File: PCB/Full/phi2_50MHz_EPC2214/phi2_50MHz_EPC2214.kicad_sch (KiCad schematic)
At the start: 37 parts, among them J4 RF_IN, J5 Conn_01x01_Pin, J6 Conn_01x01_Pin, Q1 EPC2051, Q2 EPC2051, Q3 GS61004B-MR, U1 LMG1020YFF, U1 TLV3501, U11 LMG1020YFF, U3 NC7WZ04, U5 NC7WZ04, U6 NC7WZ04, U7 NC7WZ04

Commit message: some progress on 50 MHz design
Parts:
- removed J4: RF_IN, Connector_Coaxial:SMA_Amphenol_132134-10_Vertical, symbol Connector:Conn_Coaxial
- removed Q1, Q2: EPC2051, EPCGaN:BGA-6_3x2_6.0x6.0mm, symbol Device:Q_NMOS_GSD
- removed U1: TLV3501, Package_TO_SOT_SMD:SOT-23-6, symbol MyKICAD:TLV3501
- removed U1: LMG1020YFF, GateDriver:BGA6N40P3X2_125X85X62N, symbol Driver_FET:LMG1020YFF
- added C11: C_Small, Capacitor_SMD:C_0402_1005Metric, symbol Device:C_Small
- added C12, C13, C15, C19, C20, C21, C22, C5: C, symbol Device:C_Small
- added C18: C_Small, Capacitor_SMD:CP_Elec_10x10, symbol Device:C_Small
- added C23, C24: 10U, Capacitor_SMD:C_0805_2012Metric, symbol Device:C_Small
- added C25: 100n, Capacitor_SMD:C_0603_1608Metric, symbol Device:C_Small
- added C26, C27, C28: 22U, Capacitor_SMD:C_1206_3216Metric, symbol Device:C_Small
- added C29: 100N, Capacitor_SMD:C_0603_1608Metric, symbol Device:C_Small
- added FL1: Choke, Coilcraft:IND_LPD4012-103MRB, symbol Filter:Choke_Schaffner_RN102-0.3-02-12M
- added J2: RF_IN, Connector_Coaxial:SMA_Amphenol_132134-10_Vertical, symbol Connector:Conn_Coaxial
- added L1, L2, L3, L4: L, symbol Device:L
- added L5: 2.2U, Inductor_SMD:L_Taiyo-Yuden_MD-5050, symbol Device:L_Small
- added Q2: GS61004B-MR, EPCGaN:TRANS_GS61004B-MR, symbol GS61004B-MR:GS61004B-MR
- added R13, R14: 1, Resistor_SMD:R_0402_1005Metric, symbol Device:R_Small_US
- added R7: 30K, Resistor_SMD:R_0603_1608Metric, symbol Device:R_Small_US
- added U1: TPS565242, Package_TO_SOT_SMD:SOT-563, symbol MyKICAD:TPS565242
- C1, C10, C16, C2, C3, C4: footprint Capacitor_SMD:C_0603_1608Metric_Pad1.08x0.95mm_HandSolder -> Capacitor_SMD:C_0603_1608Metric
- C14: footprint Capacitor_SMD:C_0603_1608Metric_Pad1.08x0.95mm_HandSolder -> Capacitor_SMD:C_0402_1005Metric
- C17, C8, C9: footprint Capacitor_SMD:C_0402_1005Metric_Pad0.74x0.62mm_HandSolder -> Capacitor_SMD:C_0402_1005Metric
- C6, C7: value C_Small -> C; footprint Capacitor_SMD:C_0402_1005Metric_Pad0.74x0.62mm_HandSolder -> (none)
- Q3: footprint GS61004B-MR:TRANS_GS61004B-MR -> EPCGaN:TRANS_GS61004B-MR
- R1: value 50 -> 100K; footprint Resistor_SMD:R_0603_1608Metric -> Resistor_SMD:R_0402_1005Metric
- R2: value OPEN -> 15K; footprint Resistor_SMD:R_0603_1608Metric -> Resistor_SMD:R_0402_1005Metric
- R3: value SHORT -> 220K
- U3, U5, U6, U7: footprint pcbparts:SOIC-6 -> pcbparts:nc7wz04_sc-88_SOIC-6
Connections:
- net RF_IN_4 is gone; now on net RF_IN: R1.2, U1.3 (+IN)
- net +5V: now also C8.2, C9.2, C11.2; no longer C1.1, C2.1, C3.1, C4.1, C6.1, C7.1, C8.1, C9.1, J5.1 (Pin_1), R2.1
- net GND: now also C8.1, C9.1, R2.2, C11.1, C12.2, C13.2, C15.2, C18.2, C19.2, C20.2, C21.2, C22.2, C23.2, C24.2, C25.2, C26.2, C27.2, C28.2, C29.2, C5.2, FL1.4, J2.2 (Ext), Q2.3, R7.2, U1.3 (GND), U1.4 (AGND); no longer C8.2, C9.2, R1.1, R3.2, U3.3 (A2), U5.4 (Y2), U6.4 (Y2), U7.4 (Y2)
- net at U5.6 (Y1), U6.6 (Y1), U7.6 (Y1): now also U5.4 (Y2), U6.4 (Y2), U7.4 (Y2), R14.1
- net 5V: now reaches R3.1
- net 5V: now also C26.1, C27.1, C28.1, C29.1, L5.2; no longer R2.2
- net at U11.A2 (OUTH), U11.B2 (OUTL): now also R13.1; no longer Q3.2
- net BUFF_OUT+: no longer names the net of U3.6 (Y1), U5.1 (A1), U6.1 (A1), U7.1 (A1)
- net BUFF_OUT+: now also U5.3 (A2), U6.3 (A2), U7.3 (A2)
- removed net BUFF_OUT-: U3.4 (Y2), U5.3 (A2), U6.3 (A2), U7.3 (A2)
- net RF_IN_1: no longer names the net of R1.2
- net RF_IN_1: now also R2.1, U1.5 (EN); no longer J4.1 (In)
- net RF_IN_2 renamed RF_IN
- net RF_IN: now also J4.1 (In)
- new net: Q3.2, R13.2
- new net: C13.1, C5.1, C6.1, C7.1, L2.2
- new net: C15.1, C19.1, C20.1, L1.2, L2.1, L3.1, Q2.1
- new net: L5.1, U1.2 (SW)
- new net: C12.1, C21.1, C22.1, L3.2, L4.1
- new net: R3.2, R7.1, U1.6 (FB)
- new net: J2.1 (In), L4.2
- new net +12V: C1.1, C18.1, C2.1, C3.1, C4.1, FL1.1, J5.1 (Pin_1), L1.1
- new net 12V: C23.1, C24.1, C25.1, FL1.2, R1.1, U1.1 (VIN)
- new net G: Q2.2, R14.2
- new net GND_IN: FL1.3
- no-connect marks 0 -> 2
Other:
- moved on the sheet: C1, C10, C14, C16, C17, C2, C3, C4, R1, R2, R3, U1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

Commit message: small schem progress
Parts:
- C11, C8, C9: value C_Small -> C
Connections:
- net 5V is gone; now on net +5V: C26.1, C27.1, C28.1, C29.1, L5.2, R3.1
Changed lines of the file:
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@@
 	)
 	(junction
+		(at 162.56 74.93)
+		(diameter 0)
+		(color 0 0 0 0)
+	)
+	(junction
 		(at 110.49 138.43)
 		(diameter 0)
@@
 	(wire
 		(pts
+			(xy 162.56 73.66) (xy 162.56 74.93)
+		)
+		(stroke
+			(width 0)
+			(type default)
+		)
+	)
+	(wire
+		(pts
 			(xy 217.17 148.59) (xy 217.17 149.86)
 		)
@@
 		)
 	)
-	(label "5V"
-		(at 162.56 74.93 0)
-		(fields_autoplaced yes)
-		(effects
-			(font
-				(size 1.27 1.27)
-			)
-			(justify left bottom)
-		)
-	)
 	(label "RF_IN"
 		(at 203.2 139.7 180)
@@
 			)
 		)
-		(property "Value" "C_Small"
-			(at 130.81 120.65 0)
+		(property "Value" "C"
+			(at 137.668 121.158 0)
 			(effects
 				(font
@@
 	)
 	(symbol
+		(lib_id "power:+5V")
+		(at 162.56 73.66 0)
+		(unit 1)
+		(exclude_from_sim no)
+		(in_bom yes)
+		(on_board yes)
+		(dnp no)
+		(property "Reference" "#PWR06"
+			(at 162.56 77.47 0)
+			(effects
+				(font
+					(size 1.27 1.27)
+				)
+				(hide yes)
+			)
+		)
+		(property "Value" "+5V"
+			(at 160.02 69.85 0)
+			(effects
+				(font
+					(size 1.27 1.27)
+				)
+				(justify left)
+			)
+		)
+		(property "Footprint" ""
+			(at 162.56 73.66 0)
+			(effects
+				(font
+					(size 1.27 1.27)
+				)
+				(hide yes)
+			)
+		)
+		(property "Datasheet" ""
+			(at 162.56 73.66 0)
+			(effects
+				(font
+					(size 1.27 1.27)
+				)
+				(hide yes)
+			)
+		)
+		(property "Description" ""
+			(at 162.56 73.66 0)
+			(effects
+				(font
+					(size 1.27 1.27)
+				)
+				(hide yes)
+			)
+		)
+		(pin "1"
+		)
+		(instances
+			(project "phi2_50MHz_EPC2214"
+				(path "/f0e94b14-ee89-4887-b170-fe37e788a393"
+					(reference "#PWR06")
+					(unit 1)
+				)
+			)
+		)
+	)
+	(symbol
 		(lib_id "Device:C_Small")
 		(at 124.46 33.02 0)
@@
 		(on_board yes)
 		(dnp no)
-		(fields_autoplaced yes)
 		(property "Reference" "Q2"
 			(at 231.902 81.4649 0)
@@
 		)
 		(property "Value" "GS61004B-MR"
-			(at 231.902 83.8891 0)
+			(at 227.584 83.82 0)
 			(effects
 				(font
@@
 			)
 		)
-		(property "Value" "C_Small"
-			(at 130.81 151.13 0)
+		(property "Value" "C"
+			(at 137.922 151.892 0)
 			(effects
 				(font
@@
 			)
 		)
-		(property "Value" "C_Small"
-			(at 130.81 135.89 0)
+		(property "Value" "C"
+			(at 137.922 136.398 0)
 			(effects
 				(font

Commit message: mostly finalized schematic stuff for student design board
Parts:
- removed FL1: Choke, Coilcraft:IND_LPD4012-103MRB, symbol Filter:Choke_Schaffner_RN102-0.3-02-12M
- removed Q2, Q3: GS61004B-MR, EPCGaN:TRANS_GS61004B-MR, symbol GS61004B-MR:GS61004B-MR
- removed R1: 50, Resistor_SMD:R_0603_1608Metric, symbol Device:R_Small_US
- removed R13, R14: 1, Resistor_SMD:R_0402_1005Metric, symbol Device:R_Small_US
- removed R2: OPEN, Resistor_SMD:R_0603_1608Metric, symbol Device:R_Small_US
- removed R3: SHORT, Resistor_SMD:R_0603_1608Metric, symbol Device:R_Small_US
- removed U1: TLV3501, Package_TO_SOT_SMD:SOT-23-6, symbol MyKICAD:TLV3501
- removed U11: LMG1020YFF, GateDriver:BGA6N40P3X2_125X85X62N, symbol Driver_FET:LMG1020YFF
- added C30: C, Capacitor_SMD:C_0402_1005Metric, symbol Device:C_Small
- added Q1: EPC2214, pcbparts:BGA-9_3x3_6.0x6.0mm, symbol Device:Q_NMOS_GSD
- added U2: NC7WZ04, pcbparts:nc7wz04_sc-88_SOIC-6, symbol parts:NC7WZ04
- C1: footprint Capacitor_SMD:C_0603_1608Metric -> Capacitor_SMD:CP_Elec_6.3x7.7
- C12, C13, C15, C19, C20, C21, C22, C5, C6, C7: footprint (none) -> Capacitor_SMD:C_0603_1608Metric
- C14: value C_Small -> C; footprint Capacitor_SMD:C_0402_1005Metric -> Capacitor_SMD:C_0603_1608Metric
- C16, C2, C3, C4: footprint Capacitor_SMD:C_0603_1608Metric -> Capacitor_SMD:C_1206_3216Metric
- C18: value C_Small -> 0.1u; footprint Capacitor_SMD:CP_Elec_10x10 -> Capacitor_SMD:C_0603_1608Metric
- C23, C24: value 10U -> 10u
- C26, C27, C28: value 22U -> 22u
- C29: value 100N -> 100n
- J2: value RF_IN -> RF_OUT
- L1: value L -> 20n; footprint (none) -> Coilcraft:L_Coilcraft_ZA9423
- L2: value L -> 18n; footprint (none) -> Coilcraft:Coilcraft_1212VS
- L3: value L -> 128n; footprint (none) -> Coilcraft:Coilcraft_2014VS
- L4: value L -> 259n; footprint (none) -> Coilcraft:Coilcraft_2014VS
- R1: value 100K -> 100k
- R2: value 15K -> 15k
- R3: value 220K -> 220k
- R7: value 30K -> 30k
- U1: value TPS565242 -> TPS563203
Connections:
- net 12V is gone; now on net +12V: C23.1, C24.1, C25.1, R1.1, U1.1 (VIN)
- net +12V: now also C16.1; no longer C18.1
- net +5V: now also C30.2, U2.5 (VCC); no longer C14.1, C16.1
- net G: now also U5.4 (Y2), U5.6 (Y1), U6.4 (Y2), U6.6 (Y1), U7.4 (Y2), U7.6 (Y1), Q1.1 (G), U2.4 (Y2), U2.6 (Y1)
- net GND: now also C30.1, Q1.2 (S), Q1.3 (S), Q1.8 (S), Q1.9 (S), U2.2 (GND); no longer C13.2, C14.2, C18.2, U1.4 (AGND)
- net at C5.1, C6.1, C7.1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: no longer C13.1
- net at U3.6 (Y1), U5.1 (A1), U5.3 (A2)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: now also U2.1 (A1), U2.3 (A2)
- net at C15.1, C19.1, C20.1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: now also C13.2, C14.2; no longer L1.2, L2.1
- net at L5.1, U1.2 (SW): now also C18.1
- new net: C13.1, C14.1, L1.2, L2.1, Q1.4 (D), Q1.5 (D), Q1.6 (D), Q1.7 (D)
- new net: C18.2, U1.4 (BST)
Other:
- note added: "116 pF"
- note added: "12-5 V Buck"
- note added: "140 pF"
- note added: "28 pF"
- note added: "3 nF"
- note added: "Gate Driver"
- note added: "Inputs"
- note added: "Phi-2 Power Stage"
- moved on the sheet: C1, C10, C11, C12, C15, C17, C19, C2, C20, C21, C22, C23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

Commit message: rough draft of phi 2 board
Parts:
- removed C16: C_Small, Capacitor_SMD:C_1206_3216Metric, symbol Device:C_Small
- removed C30: C, Capacitor_SMD:C_0402_1005Metric, symbol Device:C_Small
- removed U2: NC7WZ04, pcbparts:nc7wz04_sc-88_SOIC-6, symbol parts:NC7WZ04
- added D1: SMS3922, Diode_SMD:D_SOD-523, symbol Device:D
- added D2, D3, D4, D5, D6, D7, D8: RB886GT2R, Diode_SMD:D_SOD-523, symbol Device:D
- added L6: L, symbol Device:L
- C10: footprint Capacitor_SMD:C_0603_1608Metric -> Capacitor_SMD:C_0402_1005Metric
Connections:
- net +5V: now also D1.1 (K), D2.1 (K), D3.1 (K), D4.1 (K)
- net G: now also D1.2 (A), D2.2 (A), D3.2 (A), D4.2 (A), D5.1 (K), D6.1 (K), D7.1 (K), D8.1 (K), L6.2; no longer U5.4 (Y2), U5.6 (Y1), U6.4 (Y2), U6.6 (Y1), U7.4 (Y2), U7.6 (Y1)
- net GND: now also D5.2 (A), D6.2 (A), D7.2 (A), D8.2 (A)
- net D: now reaches C13.1, C14.1, L1.2, L2.1, Q1.4 (D), Q1.5 (D), Q1.6 (D), Q1.7 (D)
- net D: now also C15.1, C19.1, C20.1
- net RF_OUT: now reaches J2.1 (In), L4.2
- net at C13.2, C14.2, L3.1: no longer C15.1, C19.1, C20.1
- new net G1: L6.1, U5.4 (Y2), U5.6 (Y1), U6.4 (Y2), U6.6 (Y1), U7.4 (Y2), U7.6 (Y1)
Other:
- moved on the sheet: C10, C11, C13, C14, C15, C17, C19, C20, C8, C9, R1, R2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

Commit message: idk what i changed here
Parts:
- D2, D3, D4, D5, D6, D7, D8: value RB886GT2R -> SMS3922
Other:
- note added: "Digital resonant gate driver"
- note removed: "Gate Driver"
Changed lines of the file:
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@@
 		)
 	)
-	(text "Gate Driver"
+	(text "Digital resonant gate driver"
 		(exclude_from_sim no)
-		(at 38.354 110.236 0)
+		(at 61.722 110.744 0)
 		(effects
 			(font
@@
 			)
 		)
-		(property "Value" "RB886GT2R"
+		(property "Value" "SMS3922"
 			(at 156.21 159.004 0)
 			(effects
@@
 			)
 		)
-		(property "Value" "RB886GT2R"
+		(property "Value" "SMS3922"
 			(at 162.56 159.004 0)
 			(effects
@@
 			)
 		)
-		(property "Value" "RB886GT2R"
+		(property "Value" "SMS3922"
 			(at 149.86 145.034 0)
 			(effects
@@
 			)
 		)
-		(property "Value" "RB886GT2R"
+		(property "Value" "SMS3922"
 			(at 156.21 145.034 0)
 			(effects
@@
 			)
 		)
-		(property "Value" "RB886GT2R"
+		(property "Value" "SMS3922"
 			(at 149.86 159.004 0)
 			(effects
@@
 			)
 		)
-		(property "Value" "RB886GT2R"
+		(property "Value" "SMS3922"
 			(at 143.51 159.004 0)
 			(effects
@@
 			)
 		)
-		(property "Value" "RB886GT2R"
+		(property "Value" "SMS3922"
 			(at 162.56 145.034 0)
 			(effects

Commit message: kicad changes if i ever make a new board
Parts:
- L5: value 2.2U -> 4.7u
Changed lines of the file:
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@@
 			)
 		)
-		(property "Value" "2.2U"
+		(property "Value" "4.7u"
 			(at 101.6 73.8124 90)
 			(effects

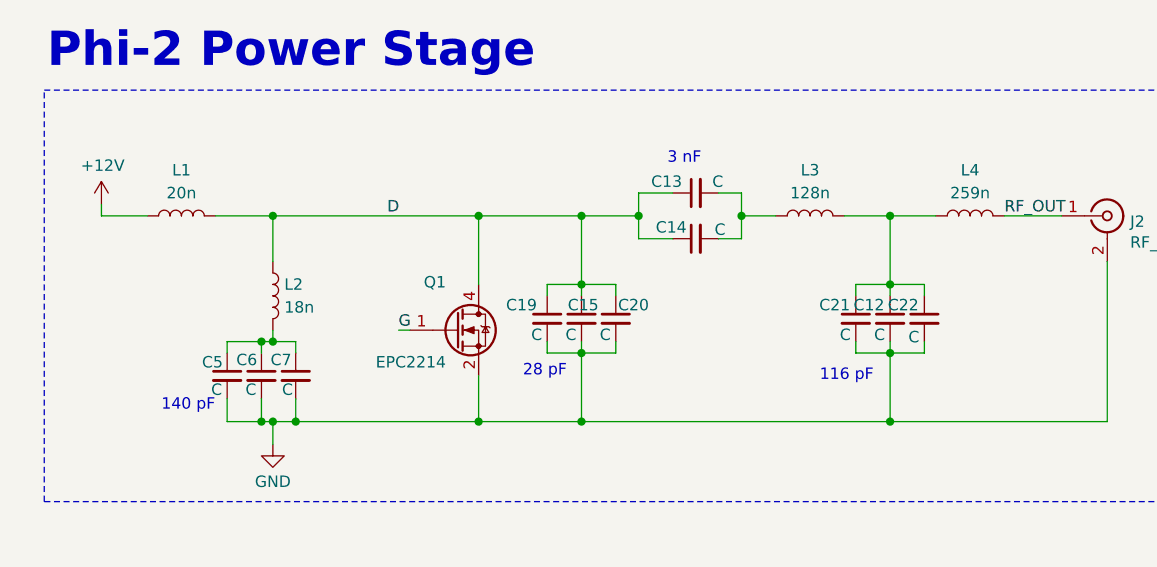
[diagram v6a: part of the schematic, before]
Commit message: matching network changes to ims design
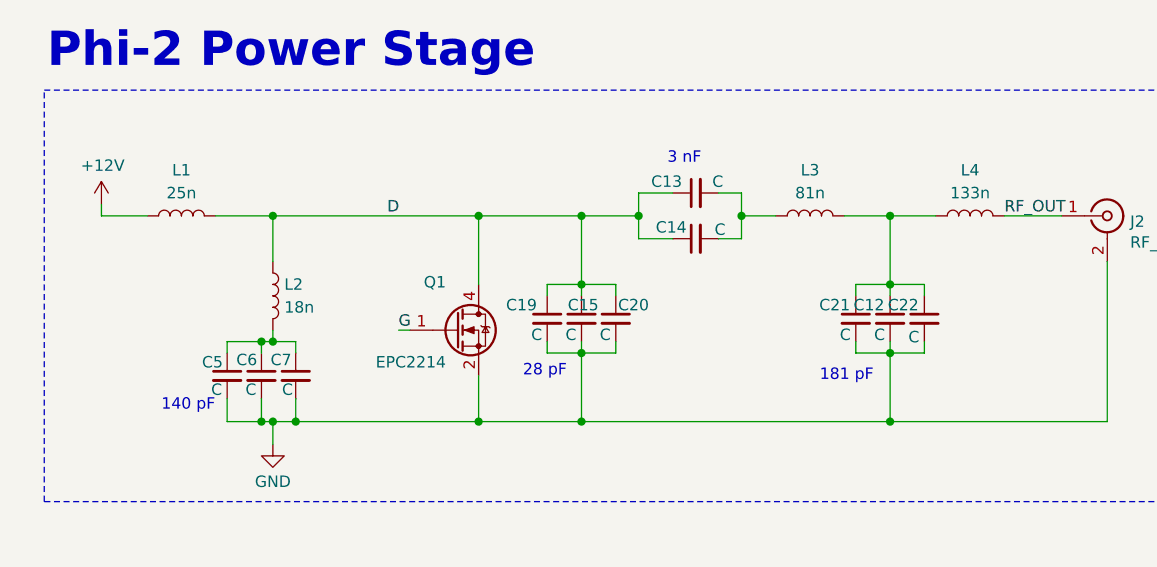
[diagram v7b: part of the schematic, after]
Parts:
- L1: value 20n -> 25n
- L3: value 128n -> 81n
- L4: value 259n -> 133n
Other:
- note added: "181 pF"
- note removed: "116 pF"
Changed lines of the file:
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@@
 		)
 	)
-	(text "116 pF"
+	(text "181 pF"
 		(exclude_from_sim no)
 		(at 275.844 115.57 0)
@@
 			)
 		)
-		(property "Value" "20n"
+		(property "Value" "25n"
 			(at 201.93 95.25 90)
 			(effects
@@
 			)
 		)
-		(property "Value" "259n"
+		(property "Value" "133n"
 			(at 289.56 95.25 90)
 			(effects
@@
 			)
 		)
-		(property "Value" "128n"
+		(property "Value" "81n"
 			(at 271.78 95.25 90)
 			(effects

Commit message: added report
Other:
- note added: "50 pF"
- note removed: "28 pF"
